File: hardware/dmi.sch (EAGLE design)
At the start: 53 parts, among them IC1 ATMEGA328-A, IC2 MAX487CSA, IC3 78SO05, IC4 LTV-354T, IC5 LTV-356T, Q1 BC337, Q2 BC337, X1 AKL_183-02, X2 AKL_183-02, X3 AKL_183-02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

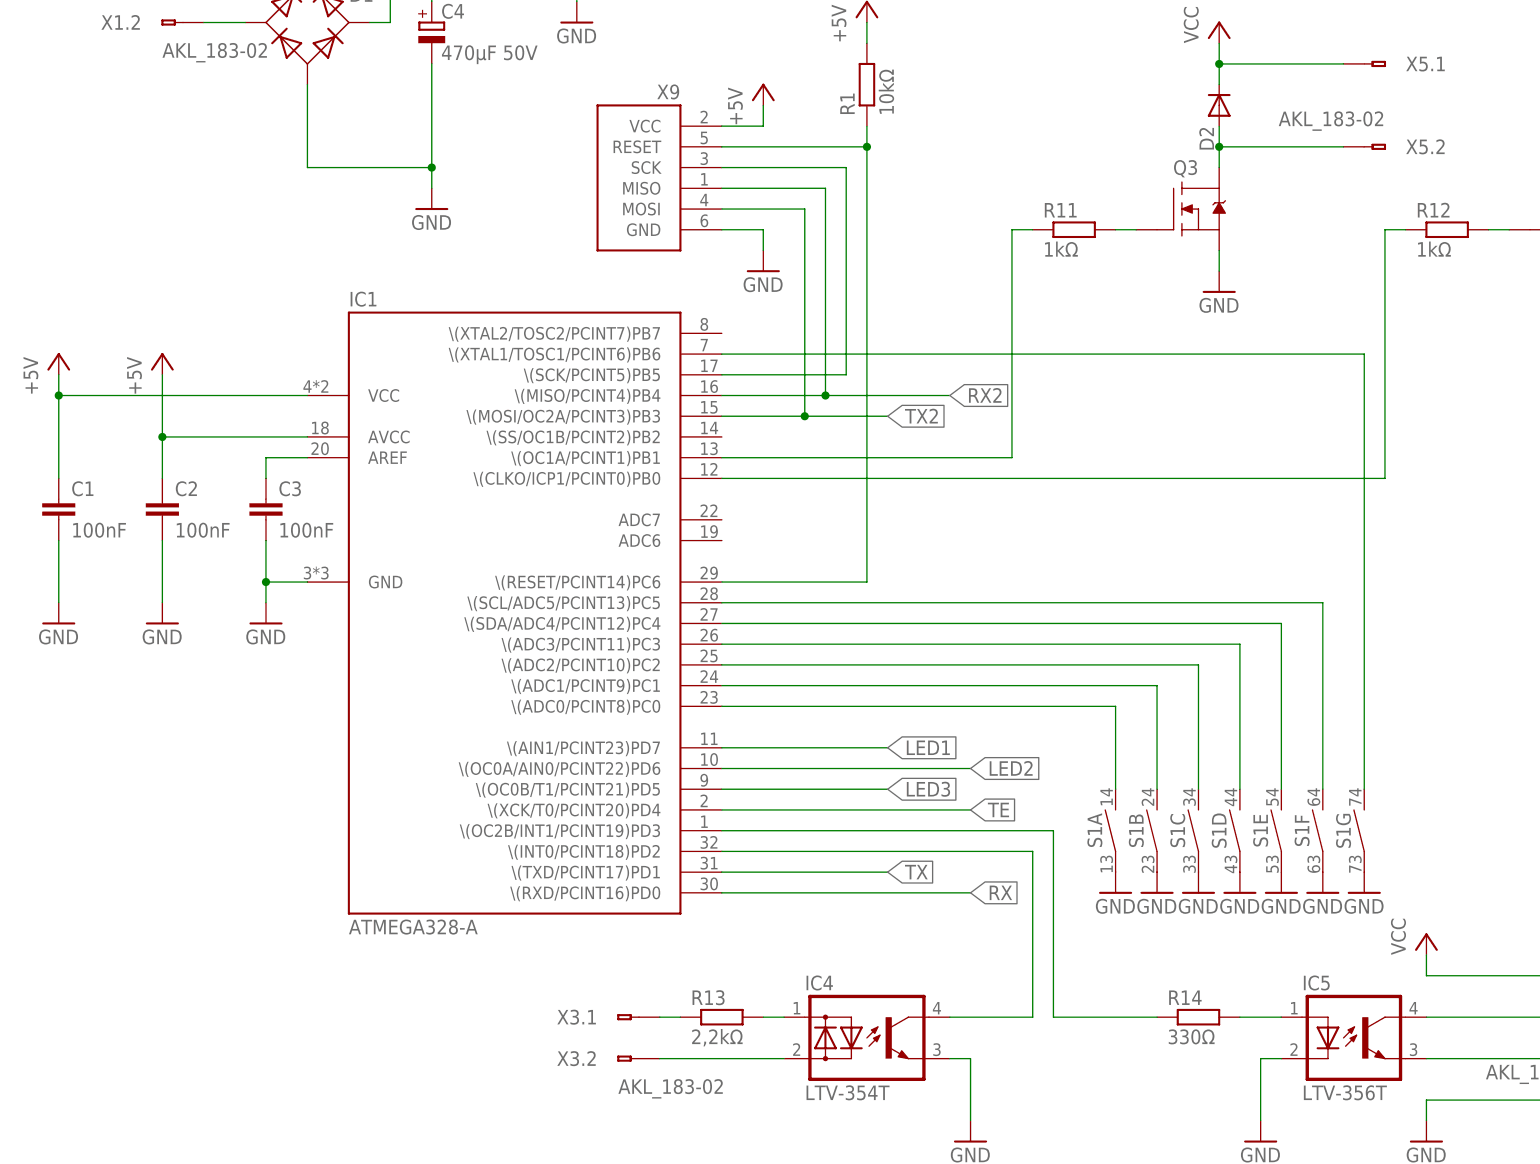
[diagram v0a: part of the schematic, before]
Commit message: Türinnenmodul überarbeitet
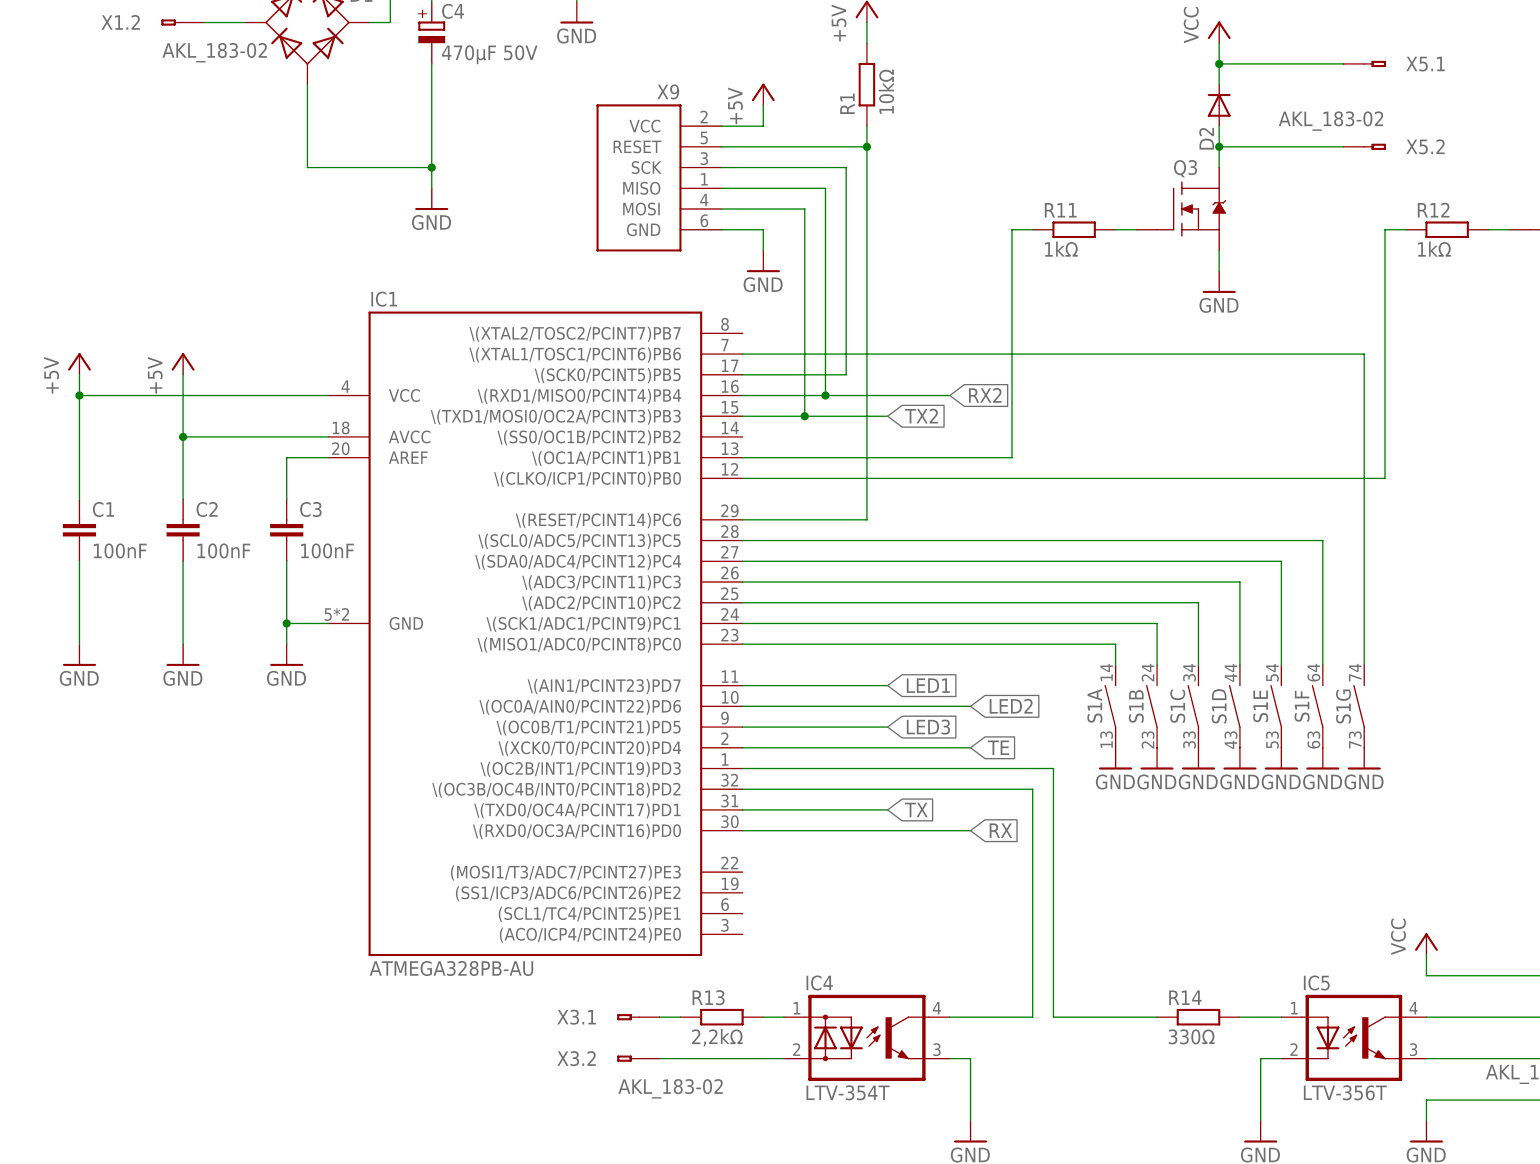
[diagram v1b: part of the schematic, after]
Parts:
- IC1: value ATMEGA328-A -> ATMEGA328PB-AU; device ic-mcu:ATMEGA328-A -> ic-mcu:ATMEGA328PB-AU
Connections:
- net N$1: now also IC1.\(OC3B/OC4B/INT0/PCINT18)PD2; no longer IC1.\(INT0/PCINT18)PD2
- net N$28: now also IC1.\(MISO1/ADC0/PCINT8)PC0; no longer IC1.\(ADC0/PCINT8)PC0
- net N$29: now also IC1.\(SCK1/ADC1/PCINT9)PC1; no longer IC1.\(ADC1/PCINT9)PC1
- net N$32: now also IC1.\(SDA0/ADC4/PCINT12)PC4; no longer IC1.\(SDA/ADC4/PCINT12)PC4
- net N$34: now also IC1.\(SCL0/ADC5/PCINT13)PC5; no longer IC1.\(SCL/ADC5/PCINT13)PC5
- net N$38: now also IC1.\(SCK0/PCINT5)PB5; no longer IC1.\(SCK/PCINT5)PB5
- net RX: now also IC1.\(RXD0/OC3A/PCINT16)PD0; no longer IC1.\(RXD/PCINT16)PD0
- net RX2: now also IC1.\(RXD1/MISO0/PCINT4)PB4; no longer IC1.\(MISO/PCINT4)PB4
- net TE: now also IC1.\(XCK0/T0/PCINT20)PD4; no longer IC1.\(XCK/T0/PCINT20)PD4
- net TX: now also IC1.\(TXD0/OC4A/PCINT17)PD1; no longer IC1.\(TXD/PCINT17)PD1
- net TX2: now also IC1.\(TXD1/MOSI0/OC2A/PCINT3)PB3; no longer IC1.\(MOSI/OC2A/PCINT3)PB3
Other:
- moved on the sheet: C1, C2, C3, S1A, S1B, S1C, S1D, S1E, S1F, S1G
